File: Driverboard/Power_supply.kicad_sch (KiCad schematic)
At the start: 40 parts

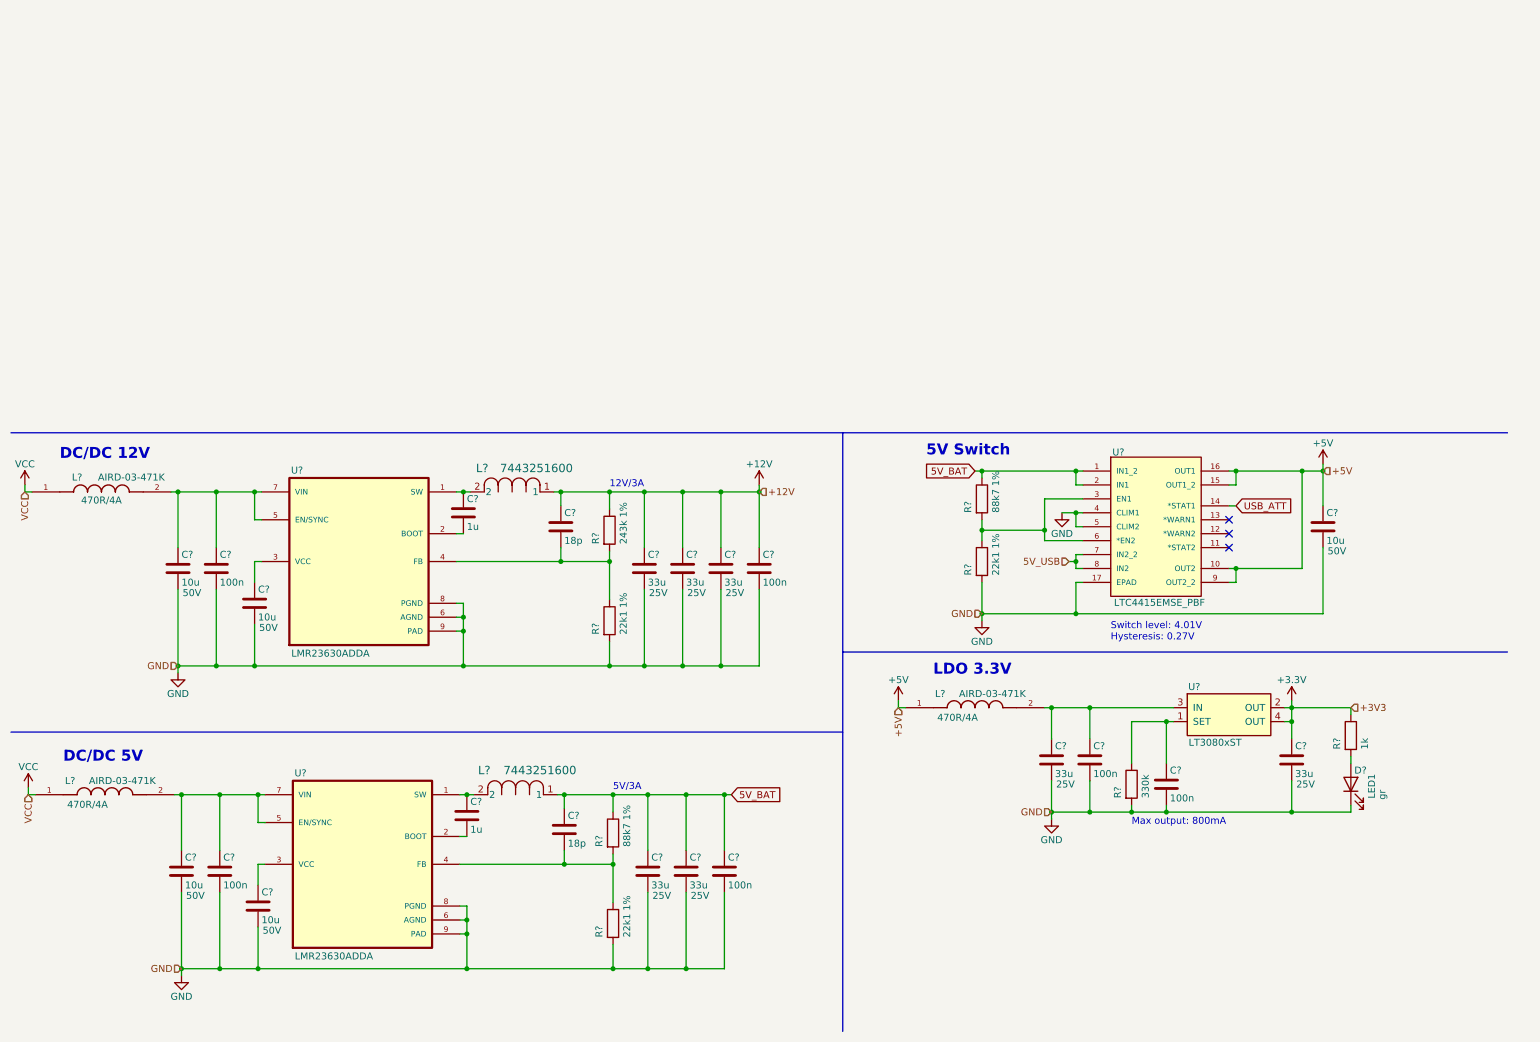
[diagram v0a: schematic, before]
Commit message: Motor Driver complete
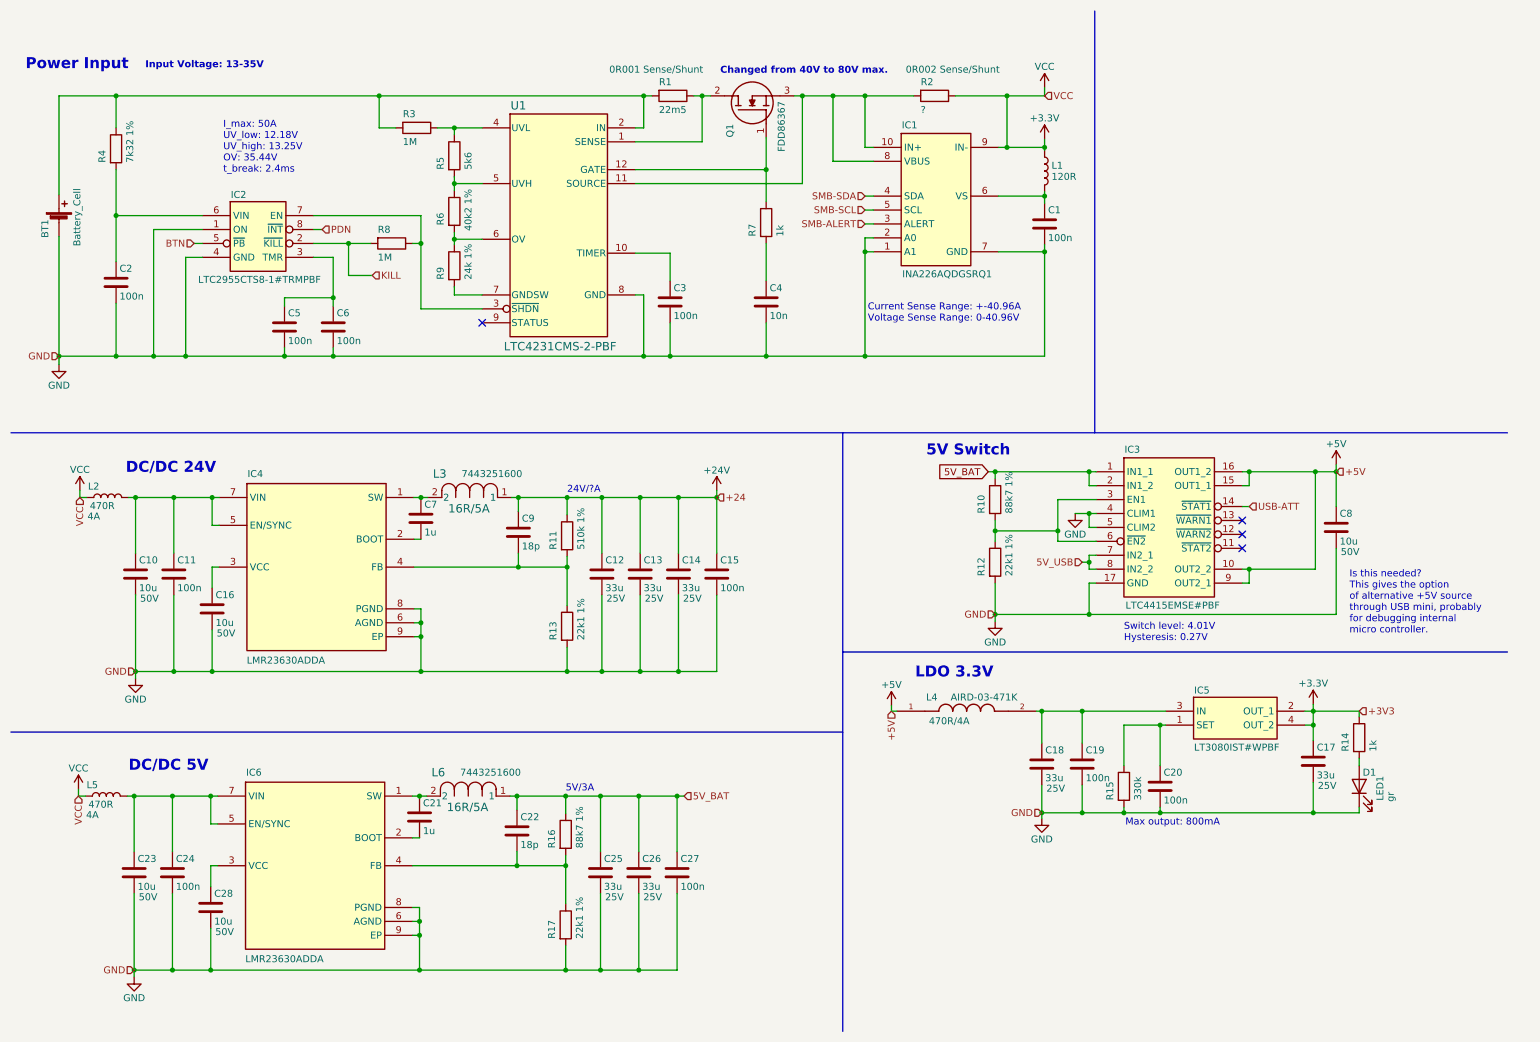
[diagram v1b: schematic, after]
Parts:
- removed L?: AIRD-03-471K, AIRD-03-471K:INDRD2200W220D2800H2100, symbol AIRD-03-471K:AIRD-03-471K
- removed L?: AIRD-03-471K, AIRD-03-471K:INDRD2200W220D2800H2100, symbol CustomSymbols:AIRD-03-471K
- removed L?: 7443251600, IND_1050-WE-HCI_WRE, symbol 2023-12-06_19-01-42:7443251600
- removed U? (x2): LMR23630ADDA, LMR23630ADDA:VREG_LM5017MR_NOPB, symbol CustomSymbols:LMR23630ADDA
- removed U?: LT3080xST, Package_TO_SOT_SMD:SOT-223, symbol Regulator_Linear:LT3080xST
- removed U?: LTC4415EMSE_PBF, LTC4415EMSE_PBF:MSOP-16_MSE, symbol CustomSymbols:LTC4415EMSE_PBF
- added BT1: Battery_Cell, symbol Device:Battery_Cell
- added C1, C2, C3, C5, C6: 100n, symbol Device:C
- added C4: 10n, symbol Device:C
- added IC1: INA226AQDGSRQ1, symbol INA226AQDGSRQ1:INA226AQDGSRQ1
- added IC2: LTC2955CTS8-1#TRMPBF, symbol LTC2955CTS8-1#TRMPBF:LTC2955CTS8-1#TRMPBF
- added IC3: LTC4415EMSE#PBF, symbol LTC4415EMSE#PBF:LTC4415EMSE#PBF
- added IC4, IC6: LMR23630ADDA, symbol LMR23630ADDA:LMR23630ADDA
- added IC5: LT3080IST#WPBF, symbol LT3080IST#WPBF:LT3080IST#WPBF
- added L1: 120R, symbol Device:L
- added L2, L5: 470R, symbol Device:L
- added L6: 16R/5A, IND_1050-WE-HCI_WRE, symbol CustomSymbols:7443251600
- added Q1: FDD86367, symbol FDD86367:FDD86367
- added R1: 22m5, symbol Device:R
- added R2: ?, symbol Device:R
- added R3, R8: 1M, symbol Device:R
- added R4: 7k32 1%, symbol Device:R
- added R5: 5k6, symbol Device:R
- added R6: 40k2 1%, symbol Device:R
- added R7: 1k, symbol Device:R
- added R9: 24k 1%, symbol Device:R
- added U1: LTC4231CMS-2-PBF, MSOP-12_MS_LIT, symbol LTC4231CMS-2#PBF:LTC4231CMS-2-PBF
- L3: renamed from L?; value 7443251600 -> 16R/5A; Name (none) -> 7443251600
- R11: renamed from R?; value 243k 1% -> 510k 1%
- gave numbers to parts that had none: 31
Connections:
- net +3.3V: now also IC1.9 (IN-), IC5.2 (OUT_1), IC5.4 (OUT_2), L1.1, L2.1, L5.1, R2.1
- net +5V: now also IC3.10 (OUT2_2), IC3.15 (OUT1_1), IC3.16 (OUT1_2), IC3.9 (OUT2_1)
- net 5V_BAT: now also IC3.1 (IN1_1), IC3.2 (IN1_2), L6.1
- net 5V_USB: now also IC3.7 (IN2_1), IC3.8 (IN2_2)
- net GND: now also BT1.2 (-), C1.2, C2.2, C3.2, C4.2, C5.2, C6.2, IC1.1 (A1), IC1.2 (A0), IC1.7 (GND), IC2.1 (ON), IC2.4 (GND), IC3.17 (GND), IC3.4 (CLIM1), IC3.5 (CLIM2), IC4.6 (AGND), IC4.8 (PGND), IC4.9 (EP), IC6.6 (AGND), IC6.8 (PGND), IC6.9 (EP), U1.8 (GND)
- net at C18.1, C19.1, L4.2: now also IC5.3 (IN)
- net at C7.1, L3.2: now also IC4.1 (SW)
- net at C7.2: now also IC4.2 (BOOT)
- net at C16.1: now also IC4.3 (VCC)
- net at C9.2, R11.2, R13.1: now also IC4.4 (FB)
- net at C10.1, C11.1: now also IC4.5 (EN/SYNC), IC4.7 (VIN), L2.2
- net at C22.2, R16.2, R17.1: now also IC6.4 (FB)
- net at C23.1, C24.1: now also IC6.5 (EN/SYNC), IC6.7 (VIN), L5.2
- net at R10.2, R12.1: now also IC3.3 (EN1), IC3.6 (~{EN2})
- net at C21.1: now also IC6.1 (SW), L6.2
- net at C21.2: now also IC6.2 (BOOT)
- net at C28.1: now also IC6.3 (VCC)
- net at C20.1, R15.1: now also IC5.1 (SET)
- net +12V renamed +24V
- new net: Q1.1 (G), R7.1, U1.12 (GATE)
- new net: Q1.2 (D), R1.1, U1.1 (SENSE)
- new net: IC1.10 (IN+), IC1.8 (VBUS), Q1.3 (S), R2.2, U1.11 (SOURCE)
- new net: C5.1, C6.1, IC2.3 (TMR)
- new net: C1.1, IC1.6 (VS), L1.2
- new net: C4.1, R7.2
- new net: BT1.1 (+), R1.2, R3.2, R4.1, U1.2 (IN)
- new net: R3.1, R5.1, U1.4 (UVL)
- new net: IC2.7 (EN), R8.1, U1.3 (~{SHDN})
- new net: C3.1, U1.10 (TIMER)
- new net: R5.2, R6.1, U1.5 (UVH)
- new net: R6.2, R9.1, U1.6 (OV)
- new net: R9.2, U1.7 (GNDSW)
- new net: C2.1, IC2.6 (VIN), R4.2
- new net BTN: IC2.5 (~{PB})
- new net KILL: IC2.2 (~{KILL}), R8.2
- new net PDN: IC2.8 (~{INT})
- new net SMB-ALERT: IC1.3 (ALERT)
- new net SMB-SCL: IC1.5 (SCL)
- new net SMB-SDA: IC1.4 (SDA)
- new net USB-ATT: IC3.14 (~{STAT1})
- no-connect marks 3 -> 4
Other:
- note added: "24V/?A"
- note added: "Changed from 40V to 80V max."
- note added: "Current Sense Range: +-40.96A Voltage Sense Range: 0-40.96V"
- note added: "DC/DC 24V"
- note added: "I_max: 50A UV_low: 12.18V UV_high: 13.25V OV: 35.44V t_break: 2.4ms"
- note added: "Input Voltage: 13-35V"
- note added: "Is this needed? This gives the option of alternative +5V source through USB mini, probably for debugging internal micro controller."
- note added: "Power Input"
- note removed: "12V/3A"
- note removed: "DC/DC 12V"
- moved on the sheet: C10, C11, C12, C13, C14, C15, C16, C17, C18, C19, C20, C21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

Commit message: WIP
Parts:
- removed C10, C16, C23, C28: 10u, symbol Device:C
- removed C11, C15, C24, C27: 100n, symbol Device:C
- removed C12, C13, C14, C25, C26: 33u, symbol Device:C
- removed C21, C7: 1u, symbol Device:C
- removed C22, C9: 18p, symbol Device:C
- removed L2, L5: 470R, symbol Device:L
- removed L3, L6: 16R/5A, IND_1050-WE-HCI_WRE, symbol CustomSymbols:7443251600
- removed R11: 510k 1%, symbol Device:R
- removed R13, R17: 22k1 1%, symbol Device:R
- removed R16: 88k7 1%, symbol Device:R
- added C10, C14, C21, C28: 100nF, symbol Device:C_Small
- added C11, C15, C22, C44: 10uF, symbol Device:C_Small
- added C12, C13, C25, C26, C9: 33uF, symbol Device:C_Small
- added C16, C23: 1uF, symbol Device:C_Small
- added C24, C7: 18pF, symbol Device:C_Small
- added L11, L3: 470uH, symbol Device:L_Small
- added L2, L5: 16uH, symbol Device:L_Small
- added R11, R16: 22k1 1%, symbol Device:R_Small
- added R13: 88k7 1%, symbol Device:R_Small
- added R35: 243k 1%, symbol Device:R_Small
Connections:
- net +3.3V: now also L11.1, L3.1
- net +5V: now also C24.1, C25.1, C26.1, C28.1, L5.2, R13.1
- net GND: now also C10.2, C11.2, C12.2, C13.2, C14.2, C15.2, C21.2, C22.2, C25.2, C26.2, C28.2, C44.2, C9.2, R11.2, R16.2
- net at IC4.3 (VCC): now also C11.1
- net at IC6.4 (FB): now also C24.2, R13.2, R16.1
- net at IC6.5 (EN/SYNC), IC6.7 (VIN): now also C15.1, C21.1, L3.2
- net at IC6.1 (SW): now also C23.1, L5.1
- net at IC4.5 (EN/SYNC), IC4.7 (VIN): now also C10.1, C44.1, L11.2
- net at IC4.4 (FB): now also C7.2, R11.1, R35.2
- net at IC4.1 (SW): now also C16.1, L2.1
- net at IC4.2 (BOOT): now also C16.2
- net at IC6.2 (BOOT): now also C23.2
- net at IC6.3 (VCC): now also C22.1
- new net +12V: C12.1, C13.1, C14.1, C7.1, C9.1, L2.2, R35.1
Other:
- note added: "12V/3A"
- note removed: "24V/?A"
- note removed: "5V/3A"
- moved on the sheet: IC4

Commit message: Powerboard v0.1, not ready for manufacturing yet
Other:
- note added: "DC/DC 12V"
- note removed: "DC/DC 24V"
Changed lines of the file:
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@@
     (stroke (width 0) (type default))
   )
-  (text "DC/DC 24V" (at 25.4 95.885 0)
+  (text "DC/DC 12V" (at 25.4 95.885 0)
     (effects (font (size 2 2) (thickness 0.254) bold) (justify left bottom))
   )
